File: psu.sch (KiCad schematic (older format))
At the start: 13 parts

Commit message: Add Test points to PSU section.
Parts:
- added TP? (x2): Test-Point-THT, footprints_generic:TestPoint-THT_C150H100, symbol gz_Test-Points:Test-Point-THT
- added TP?: Test-Point-SMT, footprints_generic:TestPoint-SMT_C100, symbol gz_Test-Points:Test-Point-SMT
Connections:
- net 3V3: now also TP?.1
- net 5V: now also TP?.1
- net at C?.1, R?.1, U?.5 (OUT): now also TP?.1
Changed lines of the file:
@@
 $EndComp
 Wire Wire Line
-	5000 1700 5800 1700
+	5000 1700 5400 1700
 Wire Wire Line
 	5800 1700 5800 1850
@@
 $EndComp
 Wire Wire Line
-	8750 1700 9250 1700
+	8750 1700 8950 1700
 Wire Wire Line
 	9250 1700 9250 1800
@@
 	1    0    0    -1
 $EndComp
+$Comp
+L gz_Test-Points:Test-Point-THT TP?
+U 1 1 6047F66A
+P 5400 1650
+F 0 "TP?" H 5457 1697 50  0000 L CNN
+F 1 "Test-Point-THT" H 5800 2000 50  0001 L CNN
+F 2 "footprints_generic:TestPoint-THT_C150H100" H 5800 2100 50  0001 L CNN
+F 3 "" H 5400 1650 50  0001 C CNN
+	1    5400 1650
+	1    0    0    -1
+$EndComp
+Wire Wire Line
+	5400 1650 5400 1700
+Connection ~ 5400 1700
+Wire Wire Line
+	5400 1700 5800 1700
+$Comp
+L gz_Test-Points:Test-Point-THT TP?
+U 1 1 60483308
+P 8950 1650
+F 0 "TP?" H 9007 1697 50  0000 L CNN
+F 1 "Test-Point-THT" H 9350 2000 50  0001 L CNN
+F 2 "footprints_generic:TestPoint-THT_C150H100" H 9350 2100 50  0001 L CNN
+F 3 "" H 8950 1650 50  0001 C CNN
+	1    8950 1650
+	1    0    0    -1
+$EndComp
+Connection ~ 8950 1700
+Wire Wire Line
+	8950 1700 9250 1700
+$Comp
+L gz_Test-Points:Test-Point-SMT TP?
+U 1 1 60483C2B
+P 10100 1700
+F 0 "TP?" V 10100 1837 50  0000 L CNN
+F 1 "Test-Point-SMT" H 10400 2050 50  0001 L CNN
+F 2 "footprints_generic:TestPoint-SMT_C100" H 10400 1950 50  0001 L CNN
+F 3 "" H 10100 1700 50  0001 C CNN
+	1    10100 1700
+	0    1    1    0
+$EndComp
+Wire Wire Line
+	8950 1650 8950 1700
+Wire Wire Line
+	10100 1700 10050 1700
+Connection ~ 10050 1700
 $EndSCHEMATC

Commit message: Add power and boot mode LED's.
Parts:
- added LED?: LiteOn-LTST-C155KGJRKT, footprints:LiteOn-LTST-C155_LEDCAV4P138_270X320X110L50X90N, symbol gz_LED-Indication-Discrete:LiteOn-LTST-C155KGJRKT
- added R?: RES-EIA0402, footprints_generic:RESC100X50X40L25NN, symbol gz_Chip-Resistors-Surface-Mount:RES-EIA0402
- R? (x2): MPN ERJ-3GEY0R00V -> ERJ3GEY0R00V
- R?: MPN ERJ-2GEJ562X -> ERJ2GEJ562X
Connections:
- net 5V: now also R?.2
- net GND: now also LED?.3 (C)
- new net: LED?.1 (A), R?.1
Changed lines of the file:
@@
 F 5 "P0.0GCT-ND" H 8450 2300 50  0001 L CNN "Vendor_PN"
 F 6 "Panasonic Electronic Components" H 9250 3000 50  0001 L CNN "Manufacturer"
-F 7 "ERJ-3GEY0R00V" H 9250 2900 50  0001 L CNN "MPN"
+F 7 "ERJ3GEY0R00V" H 9250 2900 50  0001 L CNN "MPN"
 F 8 "Resistors" H 5150 7050 50  0001 L CNN "Category"
 F 9 "Chip Resistor - Surface Mount" H 5150 7150 50  0001 L CNN "Family"
@@
 F 5 "P5.6KJCT-ND" H 7450 2750 50  0001 L CNN "Vendor_PN"
 F 6 "Panasonic Electronic Components" H 8250 3450 50  0001 L CNN "Manufacturer"
-F 7 "ERJ-2GEJ562X" H 8250 3350 50  0001 L CNN "MPN"
+F 7 "ERJ2GEJ562X" H 8250 3350 50  0001 L CNN "MPN"
 F 8 "Resistors" H 4150 7500 50  0001 L CNN "Category"
 F 9 "Chip Resistor - Surface Mount" H 4150 7600 50  0001 L CNN "Family"
@@
 F 5 "P0.0GCT-ND" H 9600 1700 50  0001 L CNN "Vendor_PN"
 F 6 "Panasonic Electronic Components" H 10400 2400 50  0001 L CNN "Manufacturer"
-F 7 "ERJ-3GEY0R00V" H 10400 2300 50  0001 L CNN "MPN"
+F 7 "ERJ3GEY0R00V" H 10400 2300 50  0001 L CNN "MPN"
 F 8 "Resistors" H 6300 6450 50  0001 L CNN "Category"
 F 9 "Chip Resistor - Surface Mount" H 6300 6550 50  0001 L CNN "Family"
@@
 	10100 1700 10050 1700
 Connection ~ 10050 1700
+$Comp
+L gz_LED-Indication-Discrete:LiteOn-LTST-C155KGJRKT LED?
+U 1 1 604DD3EB
+P 5400 3500
+F 0 "LED?" V 5359 3678 50  0000 L CNN
+F 1 "LiteOn-LTST-C155KGJRKT" H 5950 4750 50  0001 L CNN
+F 2 "footprints:LiteOn-LTST-C155_LEDCAV4P138_270X320X110L50X90N" H 5950 4650 50  0001 L CNN
+F 3 "http://optoelectronics.liteon.com/upload/download/DS22-2001-038/LTST-C155KGJRKT.pdf" H 4500 4200 50  0001 L CNN
+F 4 "Digikey" H 5950 4550 50  0001 L CNN "Vendor"
+F 5 "160-1409-1-ND" H 6350 4550 50  0001 L CNN "Vendor_PN"
+F 6 "Lite-On Inc." V 5450 3678 50  0000 L CNN "Manufacturer"
+F 7 "LTST-C155KGJRKT" V 5541 3678 50  0000 L CNN "MPN"
+F 8 "Optoelectronics" H 5950 4450 50  0001 L CNN "Category"
+F 9 "LED Indication - Discrete" H 5950 4350 50  0001 L CNN "Family"
+F 10 "Yes" H 5400 4050 50  0001 L CNN "Fit"
+	1    5400 3500
+	0    1    1    0
+$EndComp
+$Comp
+L gz_Chip-Resistors-Surface-Mount:RES-EIA0402 R?
+U 1 1 604E41D4
+P 5400 3150
+F 0 "R?" V 5550 2950 50  0000 L CNN
+F 1 "RES-EIA0402" H 6200 4050 50  0001 L CNN
+F 2 "footprints_generic:RESC100X50X40L25NN" H 2100 7500 50  0001 L CNN
+F 3 "${PANASONIC_GP_CHIP_RES_BASE}ERJ2GEJ151X" H 2100 7600 50  0001 L CNN
+F 4 "Digikey" H 5400 3150 50  0001 L CNN "Vendor"
+F 5 "P150JCT-ND" H 5400 3150 50  0001 L CNN "Vendor_PN"
+F 6 "Panasonic Electronic Components" H 6200 3850 50  0001 L CNN "Manufacturer"
+F 7 "ERJ2GEJ151X" H 6200 3750 50  0001 L CNN "MPN"
+F 8 "Resistors" H 2100 7900 50  0001 L CNN "Category"
+F 9 "Chip Resistor - Surface Mount" H 2100 8000 50  0001 L CNN "Family"
+F 10 "Yes" H 5400 3150 50  0001 L CNN "Fit"
+F 11 "150R" V 5450 2850 50  0000 L CNN "Resistance"
+F 12 "±5%" V 5450 2650 50  0000 L CNN "Tolerance"
+F 13 "1/10W" V 5350 2800 50  0000 L CNN "Power"
+F 14 "N/A" V 5536 3228 50  0001 L CNN "Voltage"
+F 15 "EIA0402" V 5250 2750 50  0000 L CNN "Package"
+	1    5400 3150
+	0    -1   -1   0
+$EndComp
+Wire Wire Line
+	5400 3350 5400 3400
+$Comp
+L gz_Power-Symbols:GND #PWR?
+U 1 1 604EC5BE
+P 5400 3750
+F 0 "#PWR?" H 5400 3500 50  0001 C CNN
+F 1 "GND" H 5405 3577 50  0000 C CNN
+F 2 "" H 5400 3750 50  0001 C CNN
+F 3 "" H 5400 3750 50  0001 C CNN
+	1    5400 3750
+	1    0    0    -1
+$EndComp
+Wire Wire Line
+	5400 3700 5400 3750
+$Comp
+L gz_Power-Symbols:5V #PWR?
+U 1 1 604EFF22
+P 5400 2900
+F 0 "#PWR?" H 5550 2850 50  0001 C CNN
+F 1 "5V" H 5405 3023 50  0000 C CNN
+F 2 "" H 5400 2900 50  0001 C CNN
+F 3 "" H 5400 2900 50  0001 C CNN
+	1    5400 2900
+	1    0    0    -1
+$EndComp
+Wire Wire Line
+	5400 2900 5400 2950
 $EndSCHEMATC

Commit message: Add current requirement to Power On LED.
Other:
- note added: "L<20mA>"
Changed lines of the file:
@@
 Wire Wire Line
 	5400 2900 5400 2950
+Text Notes 5000 3400 0    50   ~ 0
+L<20mA>
 $EndSCHEMATC

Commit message: Annotate schematic.
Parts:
- removed TP? (x2): Test-Point-THT, footprints_generic:TestPoint-THT_C150H100, symbol gz_Test-Points:Test-Point-THT
- removed TP?: Test-Point-SMT, footprints_generic:TestPoint-SMT_C100, symbol gz_Test-Points:Test-Point-SMT
- gave numbers to parts that had none: 15
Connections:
- no-connect marks 0 -> 3
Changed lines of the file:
@@
 $EndDescr
 $Comp
-L gz_USB-DVI-HDMI-Connectors:Molex-1050170001 J?
+L gz_USB-DVI-HDMI-Connectors:Molex-1050170001 J1
 U 1 1 603B74EE
 P 1450 1900
-F 0 "J?" H 1250 2750 50  0000 L CNN
+F 0 "J1" H 1250 2750 50  0000 L CNN
 F 1 "Molex-1050170001" H 1950 2850 50  0001 L CNN
 F 2 "footprints:Molex-1050170001" H 1950 2750 50  0001 L CNN
@@
 	1350 2600 1350 2500
 $Comp
-L gz_Ferrite-Beads-and-Chips:FB-EIA0603 FB?
+L gz_Ferrite-Beads-and-Chips:FB-EIA0603 FB1
 U 1 1 6043F2AE
 P 3250 1700
-F 0 "FB?" H 3050 2200 50  0000 L CNN
+F 0 "FB1" H 3050 2200 50  0000 L CNN
 F 1 "FB-EIA0603" H 3850 3100 50  0001 L CNN
 F 2 "footprints_generic:BEADC160X80X95L40N" H 3850 3000 50  0001 L CNN
@@
 Connection ~ 2350 1700
 $Comp
-L gz_Aluminum-Electrolytic-Capacitors:WE-865080245009 C?
+L gz_Aluminum-Electrolytic-Capacitors:WE-865080245009 C1
 U 1 1 60444CF8
 P 3750 1950
-F 0 "C?" H 3900 2150 50  0000 L CNN
+F 0 "C1" H 3900 2150 50  0000 L CNN
 F 1 "WE-865080245009" H 4650 3550 50  0001 L CNN
 F 2 "footprints_generic:WE-86508xx450xx_CAPAE660X770D730L255X65N" H 4650 3450 50  0001 L CNN
@@
 $EndComp
 $Comp
-L gz_Ceramic-Capacitors:CAP-EIA0603 C?
+L gz_Ceramic-Capacitors:CAP-EIA0603 C2
 U 1 1 6044A8A6
 P 5000 1950
-F 0 "C?" V 4800 2100 50  0000 L CNN
+F 0 "C2" V 4800 2100 50  0000 L CNN
 F 1 "CAP-EIA0603" H 5400 3050 50  0001 L CNN
 F 2 "footprints_generic:CAPC160X80X95L35N" H 1700 6300 50  0001 L CNN
@@
 $EndComp
 $Comp
-L gz_Ceramic-Capacitors:CAP-EIA0603 C?
+L gz_Ceramic-Capacitors:CAP-EIA0603 C3
 U 1 1 60451C07
 P 5800 1950
-F 0 "C?" V 5600 2100 50  0000 L CNN
+F 0 "C3" V 5600 2100 50  0000 L CNN
 F 1 "CAP-EIA0603" H 6200 3050 50  0001 L CNN
 F 2 "footprints_generic:CAPC160X80X95L35N" H 2500 6300 50  0001 L CNN
@@
 	5800 2050 5800 2200
 $Comp
-L gz_PMIC-Voltage-Regulators-Linear:TI-TLV75533PDBVR U?
+L gz_PMIC-Voltage-Regulators-Linear:TI-TLV75533PDBVR U1
 U 1 1 60454D63
 P 8450 1950
-F 0 "U?" H 8150 2600 50  0000 L CNN
+F 0 "U1" H 8150 2600 50  0000 L CNN
 F 1 "TI-TLV75533PDBVR" H 9200 3100 50  0001 L CNN
 F 2 "footprints:TI-TLV755_SOT23-5P95_280X145L45X40N" H 9200 3000 50  0001 L CNN
@@
 $EndComp
 $Comp
-L gz_Ceramic-Capacitors:CAP-EIA0805 C?
+L gz_Ceramic-Capacitors:CAP-EIA0805 C6
 U 1 1 6046210B
 P 9250 1900
-F 0 "C?" V 9200 2100 50  0000 L CNN
+F 0 "C6" V 9200 2100 50  0000 L CNN
 F 1 "CAP-EIA0805" H 9650 3000 50  0001 L CNN
 F 2 "footprints_generic:CAPC200X125X110L50N" H 5950 6250 50  0001 L CNN
@@
 $EndComp
 $Comp
-L gz_Chip-Resistors-Surface-Mount:RES-EIA0603 R?
+L gz_Chip-Resistors-Surface-Mount:RES-EIA0603 R3
 U 1 1 6046C6CC
 P 8450 2300
-F 0 "R?" H 8250 2400 50  0000 L CNN
+F 0 "R3" H 8250 2400 50  0000 L CNN
 F 1 "RES-EIA0603" H 9250 3200 50  0001 L CNN
 F 2 "footprints_generic:RESC160X85X55L30N" H 5150 6650 50  0001 L CNN
@@
 	8850 2000 8850 2100
 $Comp
-L gz_Ceramic-Capacitors:CAP-EIA0402 C?
+L gz_Ceramic-Capacitors:CAP-EIA0402 C5
 U 1 1 60483D8C
 P 7850 2950
-F 0 "C?" V 7700 3250 50  0000 L CNN
+F 0 "C5" V 7700 3250 50  0000 L CNN
 F 1 "CAP-EIA0402" H 8250 4050 50  0001 L CNN
 F 2 "footprints_generic:CAPC100X50X55L30N" H 4550 7300 50  0001 L CNN
@@
 $EndComp
 $Comp
-L gz_Chip-Resistors-Surface-Mount:RES-EIA0402 R?
+L gz_Chip-Resistors-Surface-Mount:RES-EIA0402 R2
 U 1 1 60486E18
 P 7450 2750
-F 0 "R?" H 7550 2550 50  0000 L CNN
+F 0 "R2" H 7550 2550 50  0000 L CNN
 F 1 "RES-EIA0402" H 8250 3650 50  0001 L CNN
 F 2 "footprints_generic:RESC100X50X40L25NN" H 4150 7100 50  0001 L CNN
@@
 	8050 1700 7400 1700
 $Comp
-L gz_Ceramic-Capacitors:CAP-EIA0603 C?
+L gz_Ceramic-Capacitors:CAP-EIA0603 C4
 U 1 1 6047D273
 P 7400 1950
-F 0 "C?" V 7200 1800 50  0000 R CNN
+F 0 "C4" V 7200 1800 50  0000 R CNN
 F 1 "CAP-EIA0603" H 7800 3050 50  0001 L CNN
 F 2 "footprints_generic:CAPC160X80X95L35N" H 4100 6300 50  0001 L CNN
@@
 	10050 1700 10050 1600
 $Comp
-L gz_TVS-Diodes:TI-TPD1E10B09DPYT ESD?
+L gz_TVS-Diodes:TI-TPD1E10B09DPYT ESD1
 U 1 1 60436474
 P 2350 1900
-F 0 "ESD?" H 2438 2037 50  0000 L CNN
+F 0 "ESD1" H 2438 2037 50  0000 L CNN
 F 1 "TI-TPD1E10B09DPYT" H 3150 2900 50  0001 L CNN
 F 2 "footprints:TI-TPD1E10B09DPYT_DIODFN2_100X60X45L25X50N" H 3150 2800 50  0001 L CNN
@@
 $EndComp
 $Comp
-L gz_Chip-Resistors-Surface-Mount:RES-EIA0603 R?
+L gz_Chip-Resistors-Surface-Mount:RES-EIA0603 R4
 U 1 1 604ED2C8
 P 9600 1700
-F 0 "R?" H 9400 2000 50  0000 L CNN
+F 0 "R4" H 9400 2000 50  0000 L CNN
 F 1 "RES-EIA0603" H 10400 2600 50  0001 L CNN
 F 2 "footprints_generic:RESC160X85X55L30N" H 6300 6050 50  0001 L CNN
@@
 $EndComp
 $Comp
-L gz_Test-Points:Test-Point-THT TP?
+L gz_Test-Points:Test-Point-THT #TP0101
 U 1 1 6047F66A
 P 5400 1650
-F 0 "TP?" H 5457 1697 50  0000 L CNN
+F 0 "#TP0101" H 5457 1697 50  0000 L CNN
 F 1 "Test-Point-THT" H 5800 2000 50  0001 L CNN
 F 2 "footprints_generic:TestPoint-THT_C150H100" H 5800 2100 50  0001 L CNN
@@
 	5400 1700 5800 1700
 $Comp
-L gz_Test-Points:Test-Point-THT TP?
+L gz_Test-Points:Test-Point-THT #TP0102
 U 1 1 60483308
 P 8950 1650
-F 0 "TP?" H 9007 1697 50  0000 L CNN
+F 0 "#TP0102" H 9007 1697 50  0000 L CNN
 F 1 "Test-Point-THT" H 9350 2000 50  0001 L CNN
 F 2 "footprints_generic:TestPoint-THT_C150H100" H 9350 2100 50  0001 L CNN
@@
 	8950 1700 9250 1700
 $Comp
-L gz_Test-Points:Test-Point-SMT TP?
+L gz_Test-Points:Test-Point-SMT #TP0103
 U 1 1 60483C2B
 P 10100 1700
-F 0 "TP?" V 10100 1837 50  0000 L CNN
+F 0 "#TP0103" V 10100 1837 50  0000 L CNN
 F 1 "Test-Point-SMT" H 10400 2050 50  0001 L CNN
 F 2 "footprints_generic:TestPoint-SMT_C100" H 10400 1950 50  0001 L CNN
@@
 Connection ~ 10050 1700
 $Comp
-L gz_LED-Indication-Discrete:LiteOn-LTST-C155KGJRKT LED?
+L gz_LED-Indication-Discrete:LiteOn-LTST-C155KGJRKT LED1
 U 1 1 604DD3EB
 P 5400 3500
-F 0 "LED?" V 5359 3678 50  0000 L CNN
+F 0 "LED1" V 5359 3678 50  0000 L CNN
 F 1 "LiteOn-LTST-C155KGJRKT" H 5950 4750 50  0001 L CNN
 F 2 "footprints:LiteOn-LTST-C155_LEDCAV4P138_270X320X110L50X90N" H 5950 4650 50  0001 L CNN
@@
 $EndComp
 $Comp
-L gz_Chip-Resistors-Surface-Mount:RES-EIA0402 R?
+L gz_Chip-Resistors-Surface-Mount:RES-EIA0402 R1
 U 1 1 604E41D4
 P 5400 3150
-F 0 "R?" V 5550 2950 50  0000 L CNN
+F 0 "R1" V 5550 2950 50  0000 L CNN
 F 1 "RES-EIA0402" H 6200 4050 50  0001 L CNN
 F 2 "footprints_generic:RESC100X50X40L25NN" H 2100 7500 50  0001 L CNN
@@
 	5400 3350 5400 3400
 $Comp
-L gz_Power-Symbols:GND #PWR?
+L gz_Power-Symbols:GND #PWR0116
 U 1 1 604EC5BE
 P 5400 3750
-F 0 "#PWR?" H 5400 3500 50  0001 C CNN
+F 0 "#PWR0116" H 5400 3500 50  0001 C CNN
 F 1 "GND" H 5405 3577 50  0000 C CNN
 F 2 "" H 5400 3750 50  0001 C CNN
@@
 	5400 3700 5400 3750
 $Comp
-L gz_Power-Symbols:5V #PWR?
+L gz_Power-Symbols:5V #PWR0117
 U 1 1 604EFF22
 P 5400 2900
-F 0 "#PWR?" H 5550 2850 50  0001 C CNN
+F 0 "#PWR0117" H 5550 2850 50  0001 C CNN
 F 1 "5V" H 5405 3023 50  0000 C CNN
 F 2 "" H 5400 2900 50  0001 C CNN
@@
 Text Notes 5000 3400 0    50   ~ 0
 L<20mA>
+NoConn ~ 1750 1800
+NoConn ~ 1750 1900
+NoConn ~ 1750 2000
 $EndSCHEMATC

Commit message: Annotate test points.
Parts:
- added TP, TP1: Test-Point-THT, footprints_generic:TestPoint-THT_C150H100, symbol gz_Test-Points:Test-Point-THT
- added TP: Test-Point-SMT, footprints_generic:TestPoint-SMT_C100, symbol gz_Test-Points:Test-Point-SMT
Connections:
- net 3V3: now also TP.1
- net 5V: now also TP1.1
- net at C6.1, R4.1, U1.5 (OUT): now also TP.1
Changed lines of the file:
@@
 $EndComp
 $Comp
-L gz_Test-Points:Test-Point-THT #TP0101
+L gz_Test-Points:Test-Point-THT TP1
 U 1 1 6047F66A
 P 5400 1650
-F 0 "#TP0101" H 5457 1697 50  0000 L CNN
+F 0 "TP1" H 5457 1697 50  0000 L CNN
 F 1 "Test-Point-THT" H 5800 2000 50  0001 L CNN
 F 2 "footprints_generic:TestPoint-THT_C150H100" H 5800 2100 50  0001 L CNN
@@
 	5400 1700 5800 1700
 $Comp
-L gz_Test-Points:Test-Point-THT #TP0102
+L gz_Test-Points:Test-Point-THT TP
 U 1 1 60483308
 P 8950 1650
-F 0 "#TP0102" H 9007 1697 50  0000 L CNN
+F 0 "TP" H 9007 1697 50  0000 L CNN
 F 1 "Test-Point-THT" H 9350 2000 50  0001 L CNN
 F 2 "footprints_generic:TestPoint-THT_C150H100" H 9350 2100 50  0001 L CNN
@@
 	8950 1700 9250 1700
 $Comp
-L gz_Test-Points:Test-Point-SMT #TP0103
+L gz_Test-Points:Test-Point-SMT TP
 U 1 1 60483C2B
 P 10100 1700
-F 0 "#TP0103" V 10100 1837 50  0000 L CNN
+F 0 "TP" V 10100 1837 50  0000 L CNN
 F 1 "Test-Point-SMT" H 10400 2050 50  0001 L CNN
 F 2 "footprints_generic:TestPoint-SMT_C100" H 10400 1950 50  0001 L CNN

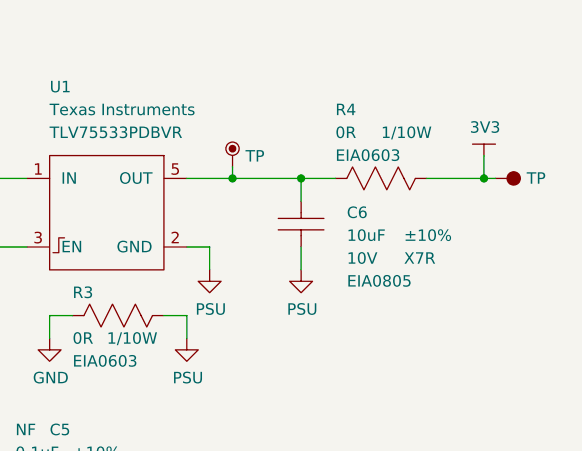
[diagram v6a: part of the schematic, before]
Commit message: Update power symbols after change to pin names; annotate.
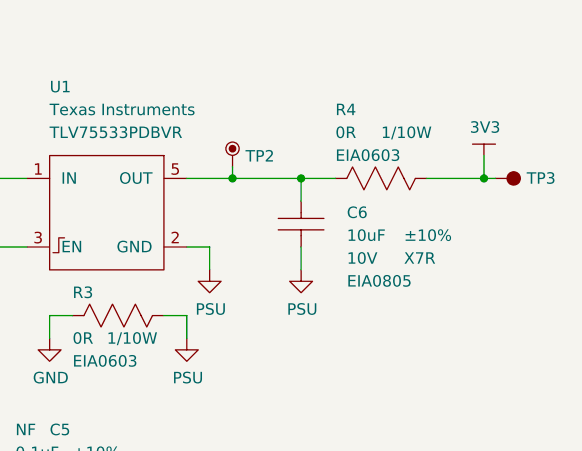
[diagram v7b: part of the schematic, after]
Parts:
- renumbered TP to TP2, TP to TP3
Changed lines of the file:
@@
 U 1 1 6046924F
 P 9250 2100
+AR Path="/6046924F" Ref="#PWR0106"  Part="1"
+AR Path="/6032FC47/6046924F" Ref="#PWR0106"  Part="1"
 F 0 "#PWR0106" H 9250 1850 50  0001 C CNN
 F 1 "PSU" H 9255 1927 50  0000 C CNN
@@
 U 1 1 6046A224
 P 8750 2400
+AR Path="/6046A224" Ref="#PWR0107"  Part="1"
+AR Path="/6032FC47/6046A224" Ref="#PWR0107"  Part="1"
 F 0 "#PWR0107" H 8750 2150 50  0001 C CNN
 F 1 "PSU" H 8755 2227 50  0000 C CNN
@@
 U 1 1 60478588
 P 8850 2100
+AR Path="/60478588" Ref="#PWR0109"  Part="1"
+AR Path="/6032FC47/60478588" Ref="#PWR0109"  Part="1"
 F 0 "#PWR0109" H 8850 1850 50  0001 C CNN
 F 1 "PSU" H 8855 1927 50  0000 C CNN
@@
 U 1 1 6047F48F
 P 7400 2100
+AR Path="/6047F48F" Ref="#PWR0110"  Part="1"
+AR Path="/6032FC47/6047F48F" Ref="#PWR0110"  Part="1"
 F 0 "#PWR0110" H 7400 1850 50  0001 C CNN
 F 1 "PSU" H 7405 1927 50  0000 C CNN
@@
 U 1 1 604A90DD
 P 7850 3150
+AR Path="/604A90DD" Ref="#PWR0111"  Part="1"
+AR Path="/6032FC47/604A90DD" Ref="#PWR0111"  Part="1"
 F 0 "#PWR0111" H 7850 2900 50  0001 C CNN
 F 1 "PSU" H 7855 2977 50  0000 C CNN
@@
 U 1 1 604B29D2
 P 5800 1600
+AR Path="/604B29D2" Ref="#PWR0112"  Part="1"
+AR Path="/6032FC47/604B29D2" Ref="#PWR0112"  Part="1"
 F 0 "#PWR0112" H 5950 1550 50  0001 C CNN
 F 1 "5V" H 5805 1723 50  0000 C CNN
@@
 U 1 1 604B3F53
 P 7400 1600
+AR Path="/604B3F53" Ref="#PWR0113"  Part="1"
+AR Path="/6032FC47/604B3F53" Ref="#PWR0113"  Part="1"
 F 0 "#PWR0113" H 7550 1550 50  0001 C CNN
 F 1 "5V" H 7405 1723 50  0000 C CNN
@@
 U 1 1 604B506C
 P 7100 2650
+AR Path="/604B506C" Ref="#PWR0114"  Part="1"
+AR Path="/6032FC47/604B506C" Ref="#PWR0114"  Part="1"
 F 0 "#PWR0114" H 7250 2600 50  0001 C CNN
 F 1 "5V" H 7105 2773 50  0000 C CNN
@@
 U 1 1 604C2C38
 P 10050 1600
+AR Path="/604C2C38" Ref="#PWR0115"  Part="1"
+AR Path="/6032FC47/604C2C38" Ref="#PWR0115"  Part="1"
 F 0 "#PWR0115" H 10200 1550 50  0001 C CNN
 F 1 "3V3" H 10055 1723 50  0000 C CNN
@@
 	5400 1700 5800 1700
 $Comp
-L gz_Test-Points:Test-Point-THT TP
+L gz_Test-Points:Test-Point-THT TP2
 U 1 1 60483308
 P 8950 1650
-F 0 "TP" H 9007 1697 50  0000 L CNN
+F 0 "TP2" H 9007 1697 50  0000 L CNN
 F 1 "Test-Point-THT" H 9350 2000 50  0001 L CNN
 F 2 "footprints_generic:TestPoint-THT_C150H100" H 9350 2100 50  0001 L CNN
@@
 	8950 1700 9250 1700
 $Comp
-L gz_Test-Points:Test-Point-SMT TP
+L gz_Test-Points:Test-Point-SMT TP3
 U 1 1 60483C2B
 P 10100 1700
-F 0 "TP" V 10100 1837 50  0000 L CNN
+F 0 "TP3" V 10100 1837 50  0000 L CNN
 F 1 "Test-Point-SMT" H 10400 2050 50  0001 L CNN
 F 2 "footprints_generic:TestPoint-SMT_C100" H 10400 1950 50  0001 L CNN
@@
 U 1 1 604EFF22
 P 5400 2900
+AR Path="/604EFF22" Ref="#PWR0117"  Part="1"
+AR Path="/6032FC47/604EFF22" Ref="#PWR0117"  Part="1"
 F 0 "#PWR0117" H 5550 2850 50  0001 C CNN
 F 1 "5V" H 5405 3023 50  0000 C CNN
